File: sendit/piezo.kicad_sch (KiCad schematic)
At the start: 3 parts, among them Q4 AO3400A

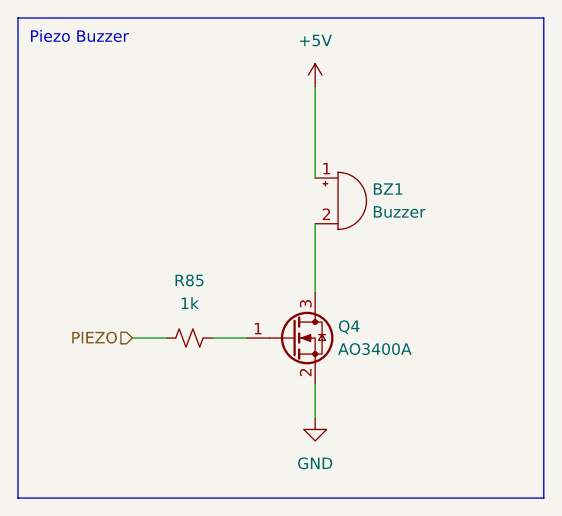
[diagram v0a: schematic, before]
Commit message: brought over the latest esp32-s3 schematic
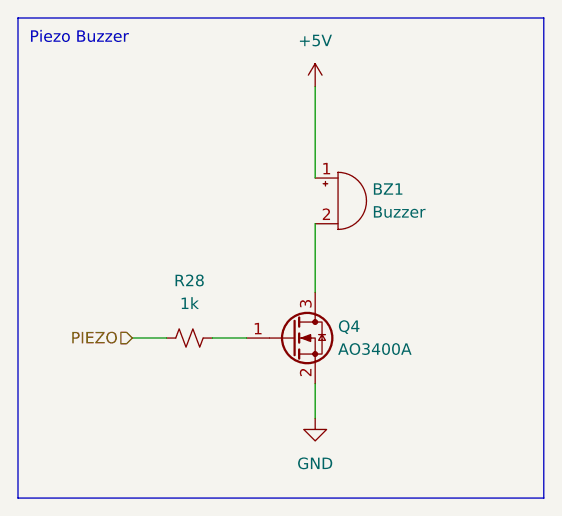
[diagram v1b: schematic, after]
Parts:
- renumbered R85 to R28
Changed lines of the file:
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@@
 		(dnp no)
 		(fields_autoplaced yes)
-		(property "Reference" "#PWR0107"
+		(property "Reference" "#PWR025"
 			(at 143.51 69.85 0)
 			(effects
@@
 			(project "sendit"
 				(path "/a355e4d0-2918-44fc-be8d-2503b84c6d6c/730ddc54-308b-4950-8f3a-2beb2098c60b"
-					(reference "#PWR0107")
+					(reference "#PWR025")
 					(unit 1)
 				)
@@
 		(dnp no)
 		(fields_autoplaced yes)
-		(property "Reference" "R85"
+		(property "Reference" "R28"
 			(at 129.54 87.63 90)
 			(effects
@@
 			(project "sendit"
 				(path "/a355e4d0-2918-44fc-be8d-2503b84c6d6c/730ddc54-308b-4950-8f3a-2beb2098c60b"
-					(reference "R85")
+					(reference "R28")
 					(unit 1)
 				)
@@
 		(dnp no)
 		(fields_autoplaced yes)
-		(property "Reference" "#PWR0108"
+		(property "Reference" "#PWR026"
 			(at 143.51 109.22 0)
 			(effects
@@
 			(project "sendit"
 				(path "/a355e4d0-2918-44fc-be8d-2503b84c6d6c/730ddc54-308b-4950-8f3a-2beb2098c60b"
-					(reference "#PWR0108")
-					(unit 1)
-				)
+					(reference "#PWR026")
+					(unit 1)
+				)

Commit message: piezo resistor
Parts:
- added R57: 100k, Resistor_SMD:R_0603_1608Metric, symbol Device:R_Small_US
- R28: value 1k -> 100R; LCSC C95781 -> (none)
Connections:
- net GND: now also R57.2
- net at Q4.1 (G), R28.1: now also R57.1
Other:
- moved on the sheet: R28
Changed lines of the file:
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@@
 		)
+	)
+	(junction
+		(at 143.51 102.87)
+		(diameter 0)
+		(color 0 0 0 0)
+	)
+	(junction
+		(at 133.35 93.98)
+		(diameter 0)
+		(color 0 0 0 0)
 	)
 	(wire
@@
 	(wire
 		(pts
+			(xy 133.35 93.98) (xy 135.89 93.98)
+		)
+		(stroke
+			(width 0)
+			(type default)
+		)
+	)
+	(wire
+		(pts
+			(xy 133.35 93.98) (xy 133.35 96.52)
+		)
+		(stroke
+			(width 0)
+			(type default)
+		)
+	)
+	(wire
+		(pts
 			(xy 143.51 66.04) (xy 143.51 76.2)
 		)
@@
 	(wire
 		(pts
-			(xy 132.08 93.98) (xy 135.89 93.98)
+			(xy 130.81 93.98) (xy 133.35 93.98)
 		)
 		(stroke
@@
 	(wire
 		(pts
-			(xy 123.19 93.98) (xy 127 93.98)
+			(xy 133.35 101.6) (xy 133.35 102.87)
+		)
+		(stroke
+			(width 0)
+			(type default)
+		)
+	)
+	(wire
+		(pts
+			(xy 121.92 93.98) (xy 125.73 93.98)
+		)
+		(stroke
+			(width 0)
+			(type default)
+		)
+	)
+	(wire
+		(pts
+			(xy 133.35 102.87) (xy 143.51 102.87)
 		)
 		(stroke
@@
 	(hierarchical_label "PIEZO"
 		(shape input)
-		(at 123.19 93.98 180)
+		(at 121.92 93.98 180)
 		(effects
 			(font
@@
 	(symbol
 		(lib_id "Device:R_Small_US")
-		(at 129.54 93.98 270)
+		(at 128.27 93.98 270)
 		(unit 1)
 		(exclude_from_sim no)
@@
 		(fields_autoplaced yes)
 		(property "Reference" "R28"
-			(at 129.54 87.63 90)
-			(effects
-				(font
-					(size 1.27 1.27)
-				)
-			)
-		)
-		(property "Value" "1k"
-			(at 129.54 90.17 90)
+			(at 128.27 87.63 90)
+			(effects
+				(font
+					(size 1.27 1.27)
+				)
+			)
+		)
+		(property "Value" "100R"
+			(at 128.27 90.17 90)
 			(effects
 				(font
@@
 		)
 		(property "Footprint" "Resistor_SMD:R_0603_1608Metric"
-			(at 129.54 93.98 0)
+			(at 128.27 93.98 0)
 			(effects
 				(font
@@
 		)
 		(property "Datasheet" "~"
-			(at 129.54 93.98 0)
+			(at 128.27 93.98 0)
 			(effects
 				(font
@@
 		)
 		(property "Description" "Resistor, small US symbol"
-			(at 129.54 93.98 0)
-			(effects
-				(font
-					(size 1.27 1.27)
-				)
-				(hide yes)
-			)
-		)
-		(property "LCSC" "C95781"
-			(at 129.54 93.98 0)
-			(effects
-				(font
-					(size 1.27 1.27)
-				)
-				(hide yes)
-			)
-		)
-		(property "ALT" ""
-			(at 129.54 93.98 0)
+			(at 128.27 93.98 0)
 			(effects
 				(font
@@
 					(unit 1)
 				)
+			)
+		)
+	)
+	(symbol
+		(lib_id "Device:R_Small_US")
+		(at 133.35 99.06 0)
+		(unit 1)
+		(exclude_from_sim no)
+		(in_bom yes)
+		(on_board yes)
+		(dnp no)
+		(fields_autoplaced yes)
+		(property "Reference" "R57"
+			(at 135.89 97.7899 0)
+			(effects
+				(font
+					(size 1.27 1.27)
+				)
+				(justify left)
+			)
+		)
+		(property "Value" "100k"
+			(at 135.89 100.3299 0)
+			(effects
+				(font
+					(size 1.27 1.27)
+				)
+				(justify left)
+			)
+		)
+		(property "Footprint" "Resistor_SMD:R_0603_1608Metric"
+			(at 133.35 99.06 0)
+			(effects
+				(font
+					(size 1.27 1.27)
+				)
+				(hide yes)
+			)
+		)
+		(property "Datasheet" "~"
+			(at 133.35 99.06 0)
+			(effects
+				(font
+					(size 1.27 1.27)
+				)
+				(hide yes)
+			)
+		)
+		(property "Description" "Resistor, small US symbol"
+			(at 133.35 99.06 0)
+			(effects
+				(font
+					(size 1.27 1.27)
+				)
+				(hide yes)
+			)
+		)
+		(pin "1"
+		)
+		(pin "2"
+		)
+		(instances
+			(project "sendit"
+				(path "/a355e4d0-2918-44fc-be8d-2503b84c6d6c/730ddc54-308b-4950-8f3a-2beb2098c60b"
+					(reference "R57")
+					(unit 1)
+				)

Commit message: bom and placement looking good.
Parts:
- BZ1: Rotation Offset (none) -> 90
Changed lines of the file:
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@@
+			)
+		)
+		(property "LCSC Part Name" ""
+			(at 140.97 93.98 0)
+			(effects
+				(font
+					(size 1.27 1.27)
+				)
+				(hide yes)
+			)
+		)
+		(property "Manufacturer" ""
+			(at 140.97 93.98 0)
+			(effects
+				(font
+					(size 1.27 1.27)
+				)
+				(hide yes)
+			)
+		)
+		(property "Manufacturer Part" ""
+			(at 140.97 93.98 0)
+			(effects
+				(font
+					(size 1.27 1.27)
+				)
+				(hide yes)
+			)
+		)
+		(property "Supplier" ""
+			(at 140.97 93.98 0)
+			(effects
+				(font
+					(size 1.27 1.27)
+				)
+				(hide yes)
+			)
+		)
+		(property "Supplier Part" ""
+			(at 140.97 93.98 0)
+			(effects
+				(font
+					(size 1.27 1.27)
+				)
+				(hide yes)
 			)
 		)
@@
 			)
 		)
+		(property "LCSC Part Name" ""
+			(at 128.27 93.98 90)
+			(effects
+				(font
+					(size 1.27 1.27)
+				)
+				(hide yes)
+			)
+		)
+		(property "Manufacturer" ""
+			(at 128.27 93.98 90)
+			(effects
+				(font
+					(size 1.27 1.27)
+				)
+				(hide yes)
+			)
+		)
+		(property "Manufacturer Part" ""
+			(at 128.27 93.98 90)
+			(effects
+				(font
+					(size 1.27 1.27)
+				)
+				(hide yes)
+			)
+		)
+		(property "Supplier" ""
+			(at 128.27 93.98 90)
+			(effects
+				(font
+					(size 1.27 1.27)
+				)
+				(hide yes)
+			)
+		)
+		(property "Supplier Part" ""
+			(at 128.27 93.98 90)
+			(effects
+				(font
+					(size 1.27 1.27)
+				)
+				(hide yes)
+			)
+		)
 		(pin "1"
 		)
@@
 			)
 		)
+		(property "LCSC Part Name" ""
+			(at 133.35 99.06 0)
+			(effects
+				(font
+					(size 1.27 1.27)
+				)
+				(hide yes)
+			)
+		)
+		(property "Manufacturer" ""
+			(at 133.35 99.06 0)
+			(effects
+				(font
+					(size 1.27 1.27)
+				)
+				(hide yes)
+			)
+		)
+		(property "Manufacturer Part" ""
+			(at 133.35 99.06 0)
+			(effects
+				(font
+					(size 1.27 1.27)
+				)
+				(hide yes)
+			)
+		)
+		(property "Supplier" ""
+			(at 133.35 99.06 0)
+			(effects
+				(font
+					(size 1.27 1.27)
+				)
+				(hide yes)
+			)
+		)
+		(property "Supplier Part" ""
+			(at 133.35 99.06 0)
+			(effects
+				(font
+					(size 1.27 1.27)
+				)
+				(hide yes)
+			)
+		)
 		(pin "1"
 		)
@@
 			(at 146.05 78.74 0)
 			(effects
+				(font
+					(size 1.27 1.27)
+				)
+				(hide yes)
+			)
+		)
+		(property "Rotation Offset" "90"
+			(at 146.05 78.74 0)
+			(effects

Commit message: cleaning up schematics a bit for design review
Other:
- title: (none) -> https://github.com/hoeken/sendit
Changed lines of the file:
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@@
 	(generator_version "9.0")
 	(paper "A4")
+	(title_block
+		(title "https://github.com/hoeken/sendit")
+		(date "2025-08-28")
+		(rev "B")
+	)
 	(rectangle
 		(start 110.49 58.42)

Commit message: more work on rev c board schematic
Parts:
- added D26: B5819W, Diode_SMD:D_SOD-123, symbol Device:D_Schottky
- BZ1: footprint yarrboard:Buzzer_FUET_9.6x9.6 -> Buzzer_Beeper:MagneticBuzzer_PUI_AT-0927-TT-6-R; LCSC C391033 -> C96256; Rotation Offset 90 -> (none)
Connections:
- net +5V: now also D26.1 (K)
- net at BZ1.2 (-), Q4.3 (D): now also D26.2 (A)
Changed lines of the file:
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@@
+	)
+	(junction
+		(at 143.51 83.82)
+		(diameter 0)
+		(color 0 0 0 0)
+	)
+	(junction
+		(at 143.51 73.66)
+		(diameter 0)
+		(color 0 0 0 0)
 	)
 	(junction
@@
 	(wire
 		(pts
+			(xy 143.51 73.66) (xy 143.51 76.2)
+		)
+		(stroke
+			(width 0)
+			(type default)
+		)
+	)
+	(wire
+		(pts
+			(xy 143.51 83.82) (xy 143.51 88.9)
+		)
+		(stroke
+			(width 0)
+			(type default)
+		)
+	)
+	(wire
+		(pts
 			(xy 143.51 99.06) (xy 143.51 102.87)
 		)
@@
 	(wire
 		(pts
-			(xy 143.51 66.04) (xy 143.51 76.2)
+			(xy 143.51 73.66) (xy 133.35 73.66)
+		)
+		(stroke
+			(width 0)
+			(type default)
+		)
+	)
+	(wire
+		(pts
+			(xy 143.51 66.04) (xy 143.51 73.66)
+		)
+		(stroke
+			(width 0)
+			(type default)
+		)
+	)
+	(wire
+		(pts
+			(xy 133.35 73.66) (xy 133.35 74.93)
 		)
 		(stroke
@@
 	(wire
 		(pts
-			(xy 143.51 81.28) (xy 143.51 88.9)
+			(xy 143.51 83.82) (xy 133.35 83.82)
+		)
+		(stroke
+			(width 0)
+			(type default)
+		)
+	)
+	(wire
+		(pts
+			(xy 133.35 83.82) (xy 133.35 82.55)
 		)
 		(stroke
@@
 		(pts
 			(xy 133.35 102.87) (xy 143.51 102.87)
+		)
+		(stroke
+			(width 0)
+			(type default)
+		)
+	)
+	(wire
+		(pts
+			(xy 143.51 81.28) (xy 143.51 83.82)
 		)
 		(stroke
@@
 	)
 	(symbol
+		(lib_id "Device:D_Schottky")
+		(at 133.35 78.74 270)
+		(unit 1)
+		(exclude_from_sim no)
+		(in_bom yes)
+		(on_board yes)
+		(dnp no)
+		(property "Reference" "D26"
+			(at 139.7 78.4225 0)
+			(effects
+				(font
+					(size 1.27 1.27)
+				)
+			)
+		)
+		(property "Value" "B5819W"
+			(at 137.16 78.4225 0)
+			(effects
+				(font
+					(size 1.27 1.27)
+				)
+			)
+		)
+		(property "Footprint" "Diode_SMD:D_SOD-123"
+			(at 133.35 78.74 0)
+			(effects
+				(font
+					(size 1.27 1.27)
+				)
+				(hide yes)
+			)
+		)
+		(property "Datasheet" "~"
+			(at 133.35 78.74 0)
+			(effects
+				(font
+					(size 1.27 1.27)
+				)
+				(hide yes)
+			)
+		)
+		(property "Description" ""
+			(at 133.35 78.74 0)
+			(effects
+				(font
+					(size 1.27 1.27)
+				)
+				(hide yes)
+			)
+		)
+		(property "Mouser" ""
+			(at 133.35 78.74 90)
+			(effects
+				(font
+					(size 1.27 1.27)
+				)
+				(hide yes)
+			)
+		)
+		(property "LCSC" ""
+			(at 133.35 78.74 0)
+			(effects
+				(font
+					(size 1.27 1.27)
+				)
+				(hide yes)
+			)
+		)
+		(property "ALT" ""
+			(at 133.35 78.74 0)
+			(effects
+				(font
+					(size 1.27 1.27)
+				)
+				(hide yes)
+			)
+		)
+		(property "LCSC Part Name" ""
+			(at 133.35 78.74 0)
+			(effects
+				(font
+					(size 1.27 1.27)
+				)
+				(hide yes)
+			)
+		)
+		(property "Manufacturer" ""
+			(at 133.35 78.74 0)
+			(effects
+				(font
+					(size 1.27 1.27)
+				)
+				(hide yes)
+			)
+		)
+		(property "Manufacturer Part" ""
+			(at 133.35 78.74 0)
+			(effects
+				(font
+					(size 1.27 1.27)
+				)
+				(hide yes)
+			)
+		)
+		(property "Supplier" ""
+			(at 133.35 78.74 0)
+			(effects
+				(font
+					(size 1.27 1.27)
+				)
+				(hide yes)
+			)
+		)
+		(property "Supplier Part" ""
+			(at 133.35 78.74 0)
+			(effects
+				(font
+					(size 1.27 1.27)
+				)
+				(hide yes)
+			)
+		)
+		(pin "1"
+		)
+		(pin "2"
+		)
+		(instances
+			(project "sendit"
+				(path "/a355e4d0-2918-44fc-be8d-2503b84c6d6c/730ddc54-308b-4950-8f3a-2beb2098c60b"
+					(reference "D26")
+					(unit 1)
+				)
+			)
+		)
+	)
+	(symbol
 		(lib_id "power:GND")
 		(at 143.51 102.87 0)
@@
 			)
 		)
-		(property "Footprint" "yarrboard:Buzzer_FUET_9.6x9.6"
+		(property "Footprint" "Buzzer_Beeper:MagneticBuzzer_PUI_AT-0927-TT-6-R"
 			(at 145.415 76.2 90)
 			(effects
@@
 			)
 		)
-		(property "LCSC" "C391033"
+		(property "LCSC" "C96256"
 			(at 146.05 78.74 0)
 			(effects
-				(font
-					(size 1.27 1.27)
-				)
-				(hide yes)
-			)
-		)
-		(property "Rotation Offset" "90"
-			(at 146.05 78.74 0)
-			(effects

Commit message: most of the work on the schematic is done.
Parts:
- renumbered D26 to D6, R28 to R21, R57 to R22
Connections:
- net +5V renamed +3.3V
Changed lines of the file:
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@@
 	)
 	(symbol
-		(lib_id "power:+5V")
+		(lib_id "power:+3.3V")
 		(at 143.51 66.04 0)
 		(unit 1)
@@
 		(on_board yes)
 		(dnp no)
-		(fields_autoplaced yes)
-		(property "Reference" "#PWR025"
+		(property "Reference" "#PWR02"
 			(at 143.51 69.85 0)
 			(effects
@@
 			)
 		)
-		(property "Value" "+5V"
+		(property "Value" "+3.3V"
 			(at 143.51 60.96 0)
 			(effects
@@
 			)
 		)
-		(property "Description" "Power symbol creates a global label with name \"+5V\""
+		(property "Description" "Power symbol creates a global label with name \"+3.3V\""
 			(at 143.51 66.04 0)
 			(effects
@@
 			(project "sendit"
 				(path "/a355e4d0-2918-44fc-be8d-2503b84c6d6c/730ddc54-308b-4950-8f3a-2beb2098c60b"
-					(reference "#PWR025")
+					(reference "#PWR02")
 					(unit 1)
 				)
@@
 		(dnp no)
 		(fields_autoplaced yes)
-		(property "Reference" "R28"
+		(property "Reference" "R21"
 			(at 128.27 87.63 90)
 			(effects
@@
 			(project "sendit"
 				(path "/a355e4d0-2918-44fc-be8d-2503b84c6d6c/730ddc54-308b-4950-8f3a-2beb2098c60b"
-					(reference "R28")
+					(reference "R21")
 					(unit 1)
 				)
@@
 		(on_board yes)
 		(dnp no)
-		(property "Reference" "D26"
+		(property "Reference" "D6"
 			(at 139.7 78.4225 0)
 			(effects
@@
 			(project "sendit"
 				(path "/a355e4d0-2918-44fc-be8d-2503b84c6d6c/730ddc54-308b-4950-8f3a-2beb2098c60b"
-					(reference "D26")
+					(reference "D6")
 					(unit 1)
 				)
@@
 		(dnp no)
 		(fields_autoplaced yes)
-		(property "Reference" "R57"
+		(property "Reference" "R22"
 			(at 135.89 97.7899 0)
 			(effects
@@
 			(project "sendit"
 				(path "/a355e4d0-2918-44fc-be8d-2503b84c6d6c/730ddc54-308b-4950-8f3a-2beb2098c60b"
-					(reference "R57")
+					(reference "R22")
 					(unit 1)
 				)
